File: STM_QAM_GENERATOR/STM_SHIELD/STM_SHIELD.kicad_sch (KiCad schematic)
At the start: 39 parts, among them J1 SMA_I, J2 SMA_Q, U2 ADA4807-2ARM, U3 ADG619, U4 ADG619, U5 LM27762, U6 ADA4807-2ARM

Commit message: STM_SHIELD_DONE
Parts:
- added C10, C11: C, Capacitor_SMD:C_0603_1608Metric_Pad1.08x0.95mm_HandSolder, symbol Device:C
- added D5, D6, D7: LED, LED_SMD:LED_0603_1608Metric_Pad1.05x0.95mm_HandSolder, symbol Device:LED
- added R24, R25, R26, R27, R32, R33, R34: R, Resistor_SMD:R_0603_1608Metric_Pad0.98x0.95mm_HandSolder, symbol Device:R
- added TP1, TP10, TP11, TP12, TP13, TP14, TP15, TP16, TP17, TP18, TP19, TP2, TP20, TP21, TP22, TP23, TP3, TP4, TP5, TP6, TP7, TP8, TP9: TestPoint, TestPoint:TestPoint_Pad_D1.0mm, symbol Connector:TestPoint
- C1, C2, C3, C4, C5, C6, C7, C8, C9: footprint (none) -> Capacitor_SMD:C_0603_1608Metric_Pad1.08x0.95mm_HandSolder
- J1, J2: footprint (none) -> Connector_Coaxial:SMA_Samtec_SMA-J-P-H-ST-EM1_EdgeMount
- R1, R10, R11, R12, R13, R14, R15, R16, R17, R18, R19, R2, R20, R21, R22, R23, R3, R4, R5, R6, R7, R8, R9: footprint (none) -> Resistor_SMD:R_0603_1608Metric_Pad0.98x0.95mm_HandSolder
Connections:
- net +3.3V: now also C10.2, C11.2, D6.2 (A), TP22.1
- net +5V: now also U5.12 (EN+), U5.8 (EN-), D5.2 (A), TP21.1
- net -3.3V: now also C10.1, C11.1, D7.1 (K)
- net ADC_I: now also TP4.1
- net ADC_Q: now also TP5.1
- net DAC_I: now also TP15.1
- net DAC_Q: now also TP14.1
- net GND: now also R24.2, R25.2, R32.2, R33.2, R34.2
- net RX_I: now also R24.1, TP2.1
- net RX_Q: now also R25.1, TP8.1
- net RX/TX: now also TP17.1, TP18.1
- net TX_I: now also R26.1, TP19.1; no longer R22.1, U6.1
- net TX_Q: now also R27.1, TP20.1; no longer R23.1, U6.7
- net at R20.1, R22.2, U6.2 (-): now also TP10.1
- net at R14.1, R15.2, U2.6 (-): now also TP6.1
- net at R10.1, R11.2, U2.2 (-): now also TP1.1
- net at R8.2, R9.1, U2.3 (+): now also TP3.1
- net at R21.1, R23.2, U6.6 (-): now also TP12.1
- net at R17.1, R19.2, U6.5 (+): now also TP13.1
- net at R12.1, R13.2, U2.5 (+): now also TP7.1
- net at R16.1, R18.2, U6.3 (+): now also TP16.1
- net at R4.1, R5.1, U5.7 (FB-): now also TP23.1
- new net: D6.1 (K), R34.1
- new net: D7.2 (A), R33.1
- new net: R22.1, R26.2, TP9.1, U6.1
- new net: D5.1 (K), R32.1
- new net: R23.1, R27.2, TP11.1, U6.7
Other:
- note removed: "TODO: 50OHM MATCH INPUT OUTPUT RESISTORS!!!"

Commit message: Added values to schematics
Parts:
- C1: value C -> 1u
- C10, C11: value C -> 100n
- C2: value C -> 4,7-10u
- C3, C4: value C -> 2.2u
- C5: value C -> 4.7u
- C6, C7, C8, C9: value C -> DNP
- R1: value R -> 10k
- R10, R14: value R -> 1.5k
- R11, R15: value R -> 11k
- R12, R16, R17, R9: value R -> 2k7
- R13, R18, R19, R8: value R -> 47k
- R2: value R -> 160k
- R20, R21: value R -> 30k
- R22, R23: value R -> 3k9
- R24, R25: value R -> DNP
- R26, R27, R6, R7: value R -> 0
- R3: value R -> 91k
- R32, R33, R34: value R -> 470
- R4: value R -> 130k
- R5: value R -> 75k
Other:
- note added: "OPA2863 drop in replacement for the ADA4807!!!"
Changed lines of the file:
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@@
 	(generator_version "9.0")
 	(paper "A4")
+	(text "OPA2863 drop in replacement for the ADA4807!!!"
+		(exclude_from_sim no)
+		(at 181.864 71.628 0)
+		(effects
+			(font
+				(size 5.08 5.08)
+			)
+		)
+	)
 	(junction
 		(at 21.59 36.83)
@@
 			)
 		)
-		(property "Value" "R"
+		(property "Value" "DNP"
 			(at 198.374 119.38 0)
 			(effects
@@
 			)
 		)
-		(property "Value" "R"
+		(property "Value" "470"
 			(at 78.74 27.686 0)
 			(effects
@@
 			)
 		)
-		(property "Value" "R"
+		(property "Value" "30k"
 			(at 68.58 110.744 0)
 			(effects
@@
 			)
 		)
-		(property "Value" "C"
+		(property "Value" "4.7u"
 			(at 104.14 43.1799 0)
 			(effects
@@
 			)
 		)
-		(property "Value" "R"
+		(property "Value" "1.5k"
 			(at 199.39 142.494 0)
 			(effects
@@
 			)
 		)
-		(property "Value" "R"
+		(property "Value" "0"
 			(at 120.904 105.156 90)
 			(effects
@@
 			)
 		)
-		(property "Value" "R"
+		(property "Value" "470"
 			(at 66.294 64.77 0)
 			(effects
@@
 			)
 		)
-		(property "Value" "C"
+		(property "Value" "2.2u"
 			(at 93.98 43.1799 0)
 			(effects
@@
 			)
 		)
-		(property "Value" "C"
+		(property "Value" "DNP"
 			(at 129.794 110.744 0)
 			(effects
@@
 			)
 		)
-		(property "Value" "R"
+		(property "Value" "160k"
 			(at 61.214 34.29 0)
 			(effects
@@
 			)
 		)
-		(property "Value" "R"
+		(property "Value" "11k"
 			(at 213.36 117.094 0)
 			(effects
@@
 			)
 		)
-		(property "Value" "R"
+		(property "Value" "30k"
 			(at 68.58 142.494 0)
 			(effects
@@
 			)
 		)
-		(property "Value" "R"
+		(property "Value" "2k7"
 			(at 54.61 138.684 0)
 			(effects
@@
 			)
 		)
-		(property "Value" "R"
+		(property "Value" "10k"
 			(at 25.4 39.37 90)
 			(effects
@@
 					(size 1.27 1.27)
 				)
-				(hide yes)
 			)
 		)
@@
 			)
 		)
-		(property "Value" "C"
+		(property "Value" "1u"
 			(at 26.67 52.0699 0)
 			(effects
@@
 			)
 		)
-		(property "Value" "R"
+		(property "Value" "470"
 			(at 15.494 45.72 0)
 			(effects
@@
 			)
 		)
-		(property "Value" "R"
+		(property "Value" "91k"
 			(at 68.326 39.37 90)
 			(effects
@@
 			)
 		)
-		(property "Value" "R"
+		(property "Value" "3k9"
 			(at 82.55 117.094 0)
 			(effects
@@
 			)
 		)
-		(property "Value" "R"
+		(property "Value" "47k"
 			(at 192.024 101.6 0)
 			(effects
@@
 		(on_board yes)
 		(dnp no)
-		(fields_autoplaced yes)
 		(property "Reference" "#PWR039"
 			(at 34.29 40.64 0)
@@
 		)
 		(property "Value" "+5V"
-			(at 26.67 40.6399 90)
+			(at 28.448 42.164 90)
 			(effects
 				(font
@@
 			)
 		)
-		(property "Value" "R"
+		(property "Value" "47k"
 			(at 61.214 101.6 0)
 			(effects
@@
 			)
 		)
-		(property "Value" "R"
+		(property "Value" "1.5k"
 			(at 199.39 110.744 0)
 			(effects
@@
 			)
 		)
-		(property "Value" "R"
+		(property "Value" "130k"
 			(at 61.468 46.99 0)
 			(effects
@@
 			)
 		)
-		(property "Value" "R"
+		(property "Value" "0"
 			(at 93.98 108.204 0)
 			(effects
@@
 			)
 		)
-		(property "Value" "C"
+		(property "Value" "DNP"
 			(at 129.794 141.224 0)
 			(effects
@@
 			)
 		)
-		(property "Value" "R"
+		(property "Value" "2k7"
 			(at 185.42 106.934 0)
 			(effects
@@
 			)
 		)
-		(property "Value" "R"
+		(property "Value" "DNP"
 			(at 198.374 151.13 0)
 			(effects
@@
 			)
 		)
-		(property "Value" "R"
+		(property "Value" "0"
 			(at 93.98 139.954 0)
 			(effects
@@
 			)
 		)
-		(property "Value" "C"
-			(at 56.134 61.214 0)
+		(property "Value" "4,7-10u"
+			(at 53.848 61.214 0)
 			(effects
 				(font
@@
 			)
 		)
-		(property "Value" "R"
+		(property "Value" "11k"
 			(at 213.36 148.844 0)
 			(effects
@@
 			)
 		)
-		(property "Value" "R"
+		(property "Value" "47k"
 			(at 192.024 133.35 0)
 			(effects
@@
 			)
 		)
-		(property "Value" "R"
+		(property "Value" "3k9"
 			(at 82.55 148.844 0)
 			(effects
@@
 			)
 		)
-		(property "Value" "C"
+		(property "Value" "2.2u"
 			(at 82.55 43.1799 0)
 			(effects
@@
 			)
 		)
-		(property "Value" "C"
-			(at 240.284 127.254 0)
+		(property "Value" "100n"
+			(at 238.252 127.254 0)
 			(effects
 				(font
@@
 			)
 		)
-		(property "Value" "R"
+		(property "Value" "75k"
 			(at 68.834 44.196 90)
 			(effects
@@
 			)
 		)
-		(property "Value" "R"
+		(property "Value" "0"
 			(at 120.904 135.636 90)
 			(effects
@@
 			)
 		)
-		(property "Value" "C"
+		(property "Value" "DNP"
 			(at 117.602 110.744 0)
 			(effects
@@
 			)
 		)
-		(property "Value" "C"
+		(property "Value" "100n"
 			(at 23.114 125.984 0)
 			(effects
@@
 			)
 		)
-		(property "Value" "R"
+		(property "Value" "2k7"
 			(at 54.61 106.934 0)
 			(effects
@@
 			)
 		)
-		(property "Value" "R"
+		(property "Value" "47k"
 			(at 61.214 133.35 0)
 			(effects
@@
 			)
 		)
-		(property "Value" "R"
+		(property "Value" "2k7"
 			(at 185.42 138.684 0)
 			(effects
@@
 			)
 		)
-		(property "Value" "C"
+		(property "Value" "DNP"
 			(at 117.602 141.224 0)
 			(effects

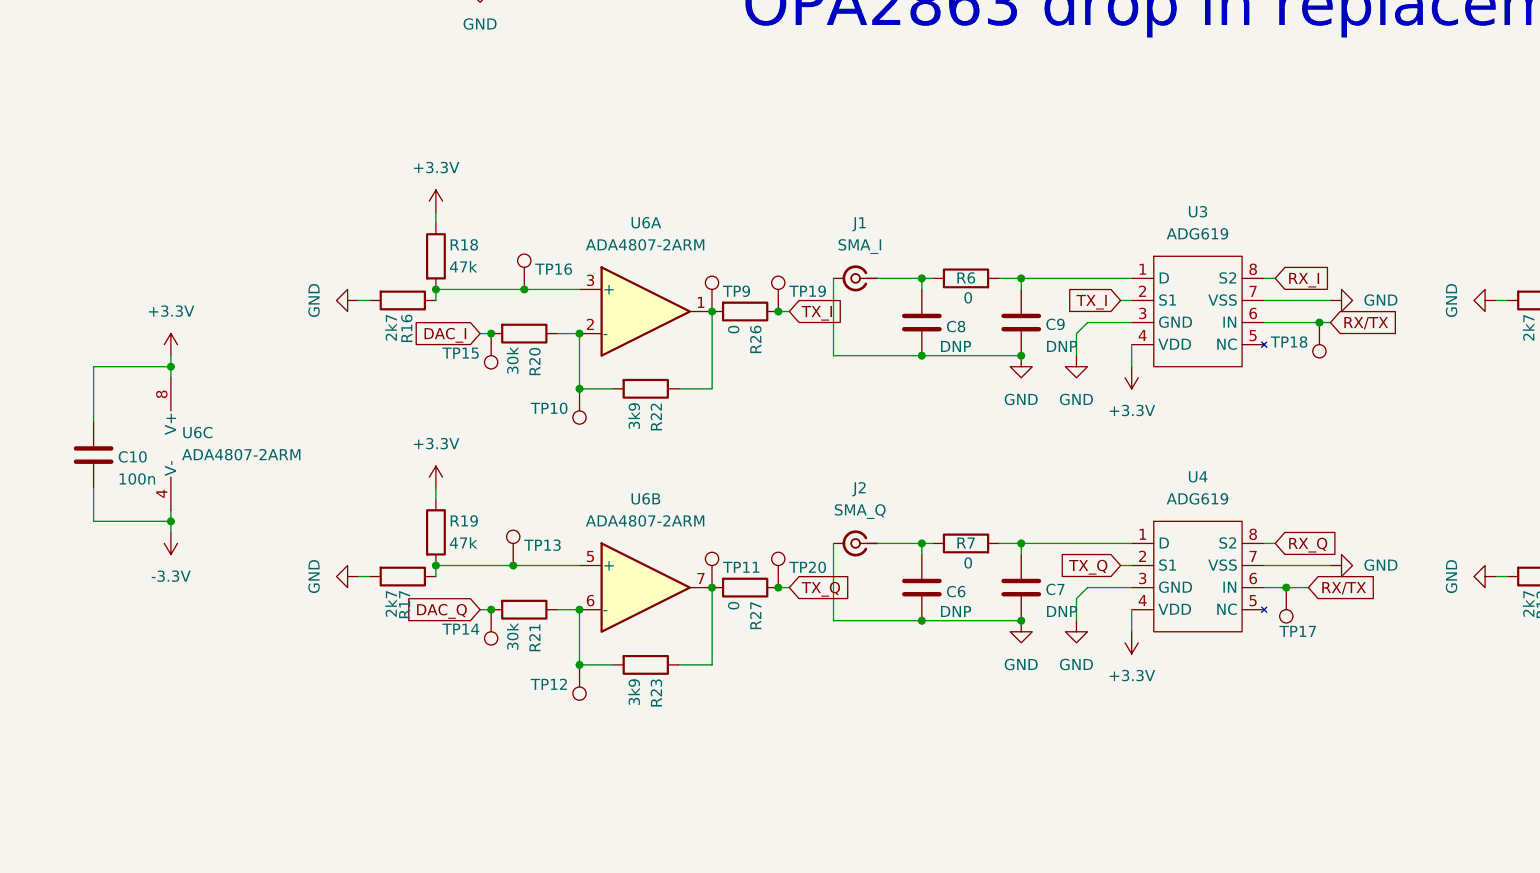
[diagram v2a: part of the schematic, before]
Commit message: STM ADC/DAC test scripts calibrated
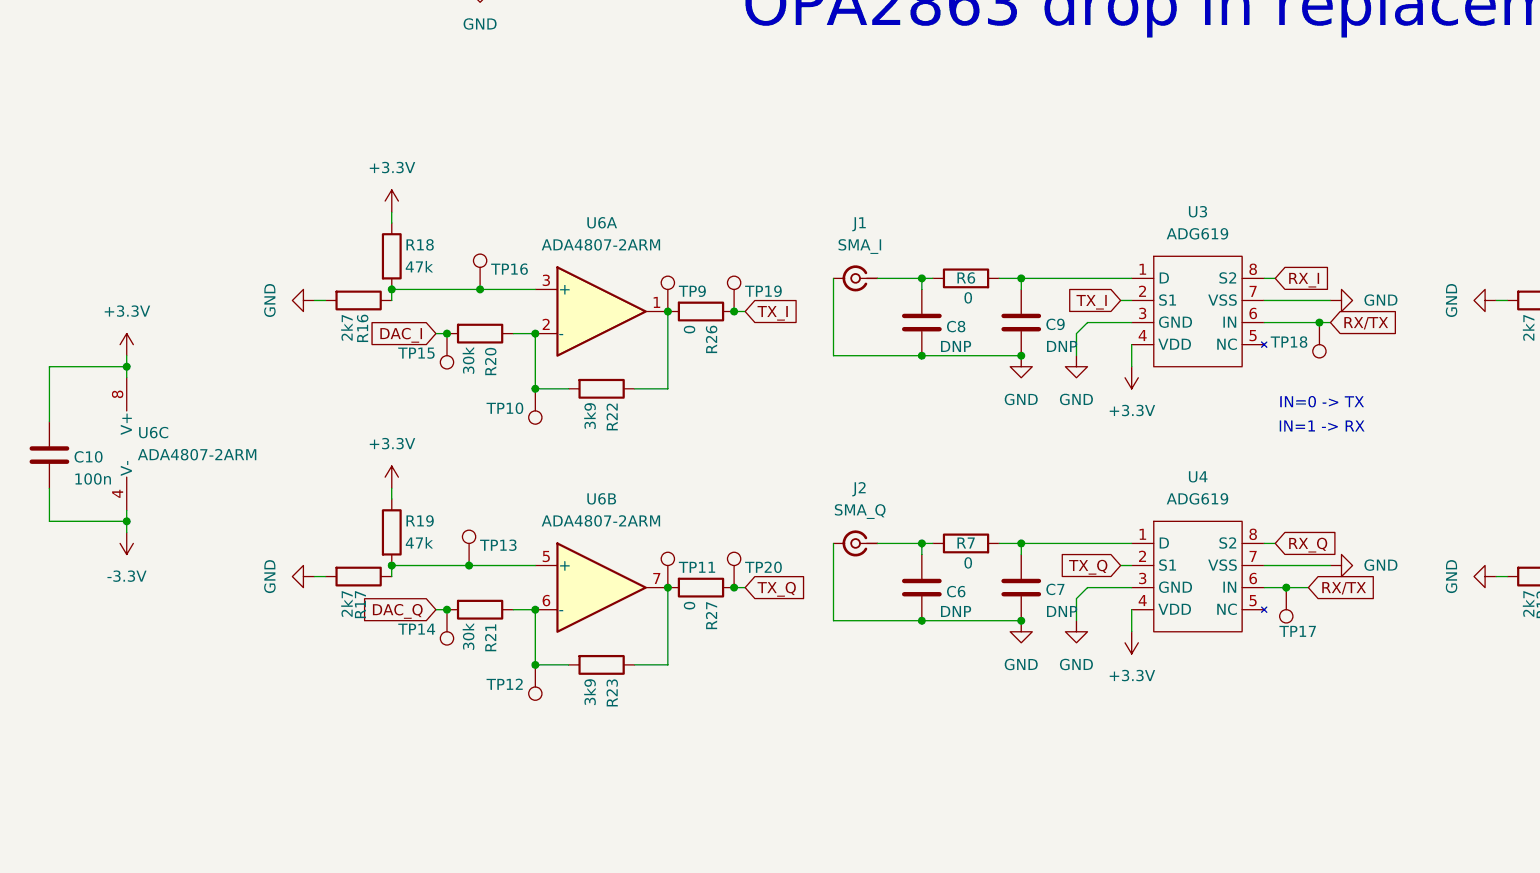
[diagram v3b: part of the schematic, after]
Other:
- note added: "IN=0 -> TX"
- note added: "IN=1 -> RX"
- moved on the sheet: C10, R16, R17, R18, R19, R20, R21, R22, R23, R26, R27, TP10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
